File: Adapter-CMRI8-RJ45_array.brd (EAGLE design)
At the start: 100.6 x 107.6 mm, 96 parts

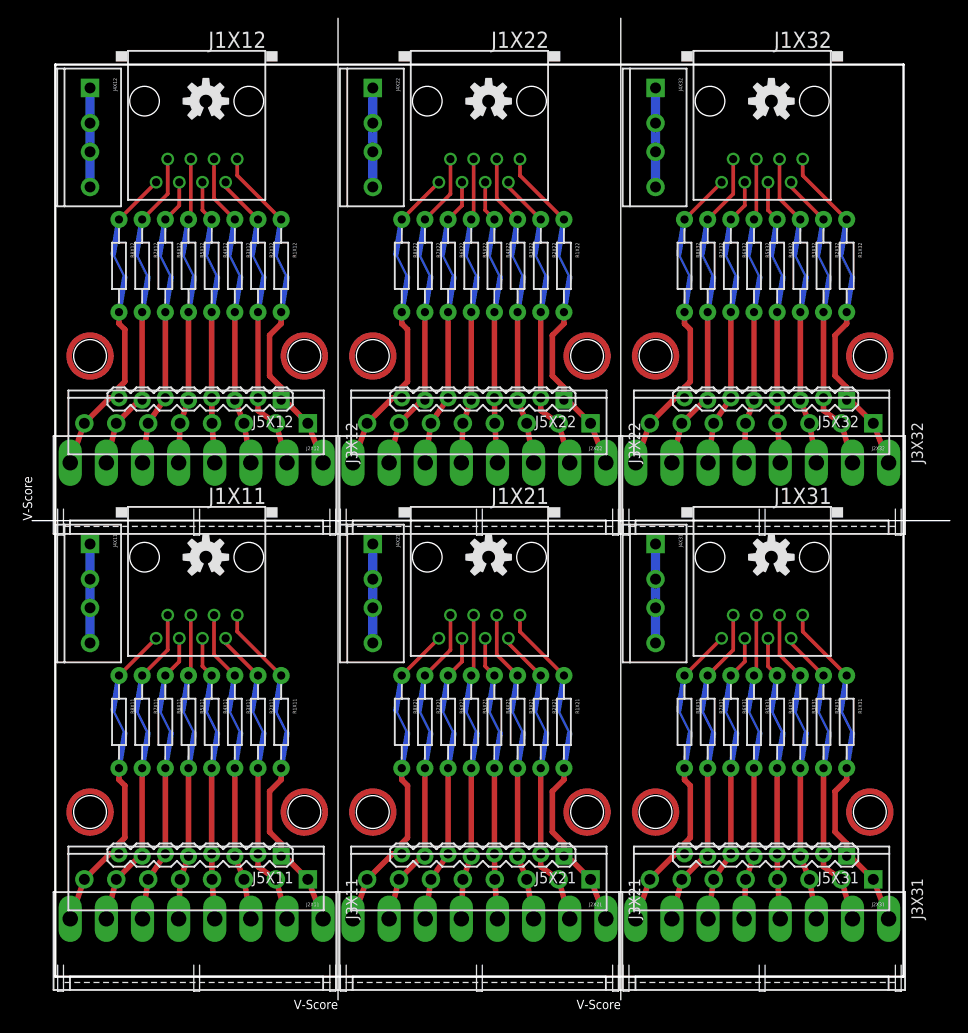
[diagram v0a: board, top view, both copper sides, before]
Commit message: V5.0 added SPDT frog power
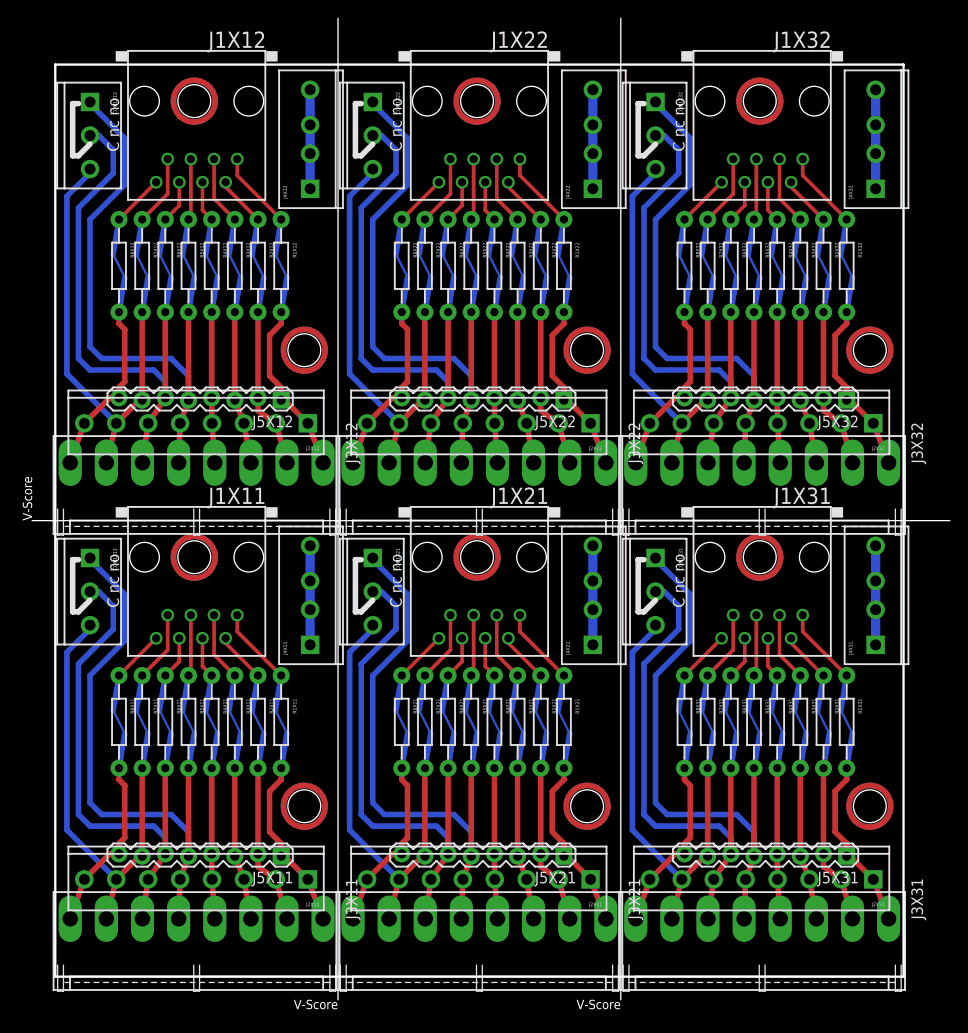
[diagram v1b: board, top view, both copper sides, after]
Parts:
- added CON1X11, CON1X12, CON1X21, CON1X22, CON1X31, CON1X32: CONNECTOR-M033.5MM-LOCK, SPCoast:SCREWTERMINAL-3.5MM-3_LOCK.007S
- J1X11, J1X12, J1X21, J1X22, J1X31, J1X32: value (none) -> RJ45
- M1X11, M1X12, M1X21, M1X22, M1X31, M1X32, M2X11, M2X12, M2X21, M2X22, M2X31, M2X32: value (none) -> MOUNTINGHOLE
- U$1X11, U$1X12, U$1X21, U$1X22, U$1X31, U$1X32: value (none) -> DOC-OSHW-LOGO-L; device SPCoast:OSHW-LOGO-M -> SPCoast:OSHW-LOGO-L
- moved M1X11 30.2 mm to (15.2, 46.0)
- moved M1X21 30.2 mm to (46.2, 46.0)
- moved M1X12 30.2 mm to (15.2, 96.0)
- moved M1X22 30.2 mm to (46.2, 96.0)
- moved M1X31 30.2 mm to (77.2, 46.0)
- moved M1X32 30.2 mm to (77.2, 96.0)
- moved J4X11 26.4 mm to (27.9, 36.6), turned to 90 degrees
- moved J4X12 26.4 mm to (27.9, 86.6), turned to 90 degrees
- moved J4X21 26.4 mm to (58.9, 36.6), turned to 90 degrees
- moved J4X22 26.4 mm to (58.9, 86.6), turned to 90 degrees
- moved J4X31 26.4 mm to (89.9, 36.6), turned to 90 degrees
- moved J4X32 26.4 mm to (89.9, 86.6), turned to 90 degrees
- moved U$1X31 1.27 mm to (77.2, 46.0)
- moved U$1X32 1.27 mm to (77.2, 96.0)
- moved U$1X11 1.27 mm to (15.2, 46.0)
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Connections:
- net L5X11: now also CON1X11.1
- net L5X12: now also CON1X12.1
- net L5X21: now also CON1X21.1
- net L5X22: now also CON1X22.1
- net L5X31: now also CON1X31.1
- net L5X32: now also CON1X32.1
- net L6X11: now also CON1X11.2
- net L6X12: now also CON1X12.2
- net L6X21: now also CON1X21.2
- net L6X22: now also CON1X22.2
- net L6X31: now also CON1X31.2
- net L6X32: now also CON1X32.2
- net L7X11: now also CON1X11.3
- net L7X12: now also CON1X12.3
- net L7X21: now also CON1X21.3
- net L7X22: now also CON1X22.3
- net L7X31: now also CON1X31.3
- net L7X32: now also CON1X32.3
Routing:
- net L5X32: track 34.0 -> 78.7 mm
- net L5X31: track 34.0 -> 78.7 mm
- net L5X22: track 34.0 -> 78.7 mm
- net L5X12: track 34.0 -> 78.7 mm
- net L5X11: track 34.0 -> 78.7 mm
- net L5X21: track 34.0 -> 78.7 mm
- net L6X22: track 32.4 -> 72.4 mm
- net L6X21: track 32.4 -> 72.4 mm
- net L6X12: track 32.4 -> 72.4 mm
- net L6X11: track 32.4 -> 72.4 mm
- net L6X32: track 32.4 -> 72.4 mm
- net L6X31: track 32.4 -> 72.4 mm
- net L7X31: track 36.3 -> 67.1 mm
- net L7X11: track 36.3 -> 67.1 mm
- net L7X21: track 36.3 -> 67.1 mm
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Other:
- board text added: "2020.06"
- board text added: "C nc no"
- board text added: "CON1"
- board text added: "Frog Pwr"
- board text added: "no nc C"
- board text added: "v5.0"
- board text removed: "0.156""
- board text removed: "2018.12"
- board text removed: "Resistor"
- board text removed: "v4.0"

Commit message: added values for connectors
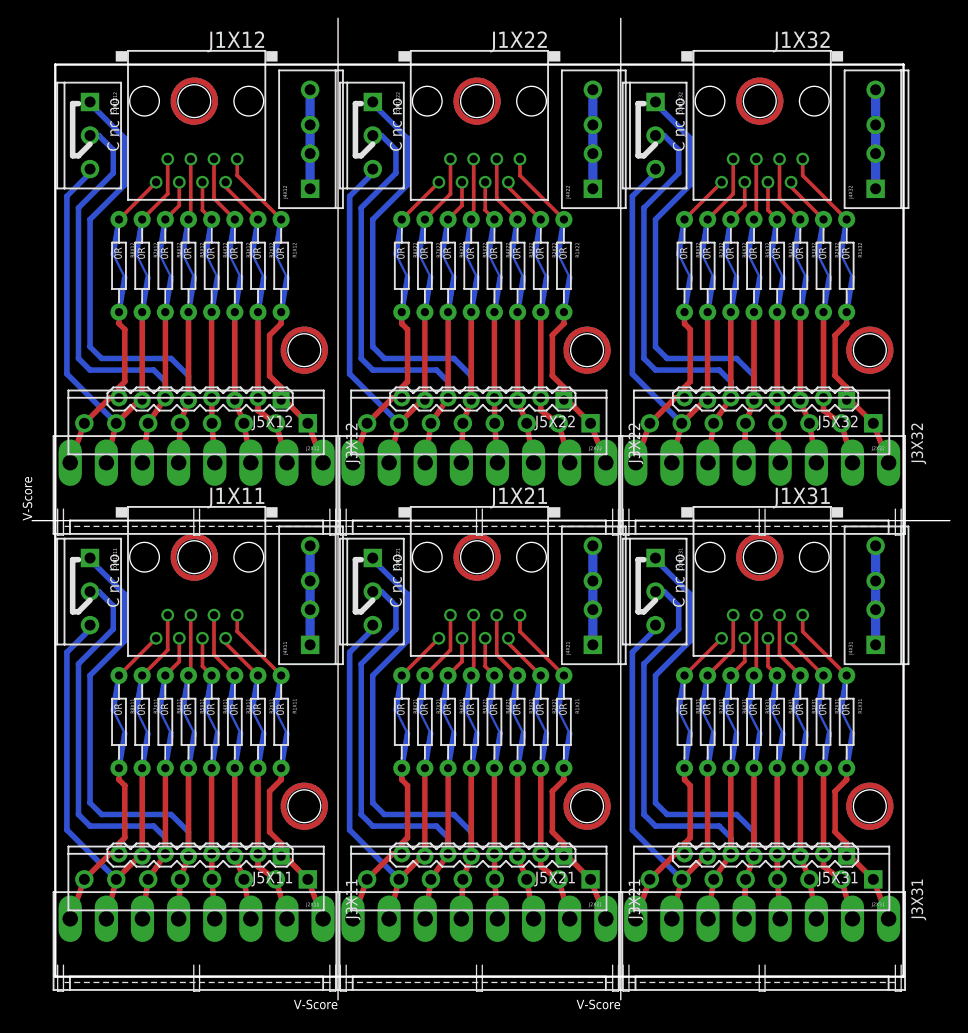
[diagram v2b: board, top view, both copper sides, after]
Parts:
- J2X11, J2X12, J2X21, J2X22, J2X31, J2X32, J4X11, J4X12, J4X21, J4X22, J4X31, J4X32: value (none) -> 3.5mm
- J5X11, J5X12, J5X21, J5X22, J5X31, J5X32: value (none) -> 0.100
- R1X11, R1X12, R1X21, R1X22, R1X31, R1X32, R2X11, R2X12, R2X21, R2X22, R2X31, R2X32, R3X11, R3X12, R3X21, R3X22, R3X31, R3X32, R4X11, R4X12, R4X21, R4X22, R4X31, R4X32, R5X11, R5X12, R5X21, R5X22, R5X31, R5X32, R6X11, R6X12, R6X21, R6X22, R6X31, R6X32, R7X11, R7X12, R7X21, R7X22, R7X31, R7X32, R8X11, R8X12, R8X21, R8X22, R8X31, R8X32: value (none) -> 0R

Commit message: added values for connectors
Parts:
- J3X11, J3X12, J3X21, J3X22, J3X31, J3X32: value (none) -> 0.156
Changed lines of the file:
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@@
 <element name="J1X11" library="SPCoast" package="RJ45-NO-SHIELD" value="RJ45" x="15.5" y="45.99" rot="R180"/>
 <element name="J2X11" library="SPCoast" package="SCREWTERMINAL-3.5MM-8" value="3.5mm" x="27.686" y="10.668" rot="R180"/>
-<element name="J3X11" library="SPCoast" package="KK-156-8-F" value="" x="15.5" y="6.35" rot="R180"/>
+<element name="J3X11" library="SPCoast" package="KK-156-8-F" value="0.156" x="15.5" y="6.35" rot="R180"/>
 <element name="J4X11" library="SPCoast" package="SCREWTERMINAL-3.5MM-4_LOCK" value="3.5mm" x="27.94" y="36.56" rot="R90"/>
 <element name="J5X11" library="SPCoast" package="1X08_LOCK" value="0.100" x="24.765" y="13.335" rot="R180"/>
@@
 <element name="J1X12" library="SPCoast" package="RJ45-NO-SHIELD" value="RJ45" x="15.5" y="95.99" rot="R180"/>
 <element name="J2X12" library="SPCoast" package="SCREWTERMINAL-3.5MM-8" value="3.5mm" x="27.686" y="60.668" rot="R180"/>
-<element name="J3X12" library="SPCoast" package="KK-156-8-F" value="" x="15.5" y="56.35" rot="R180"/>
+<element name="J3X12" library="SPCoast" package="KK-156-8-F" value="0.156" x="15.5" y="56.35" rot="R180"/>
 <element name="J4X12" library="SPCoast" package="SCREWTERMINAL-3.5MM-4_LOCK" value="3.5mm" x="27.94" y="86.56" rot="R90"/>
 <element name="J5X12" library="SPCoast" package="1X08_LOCK" value="0.100" x="24.765" y="63.335" rot="R180"/>
@@
 <element name="J1X21" library="SPCoast" package="RJ45-NO-SHIELD" value="RJ45" x="46.5" y="45.99" rot="R180"/>
 <element name="J2X21" library="SPCoast" package="SCREWTERMINAL-3.5MM-8" value="3.5mm" x="58.686" y="10.668" rot="R180"/>
-<element name="J3X21" library="SPCoast" package="KK-156-8-F" value="" x="46.5" y="6.35" rot="R180"/>
+<element name="J3X21" library="SPCoast" package="KK-156-8-F" value="0.156" x="46.5" y="6.35" rot="R180"/>
 <element name="J4X21" library="SPCoast" package="SCREWTERMINAL-3.5MM-4_LOCK" value="3.5mm" x="58.94" y="36.56" rot="R90"/>
 <element name="J5X21" library="SPCoast" package="1X08_LOCK" value="0.100" x="55.765" y="13.335" rot="R180"/>
@@
 <element name="J1X22" library="SPCoast" package="RJ45-NO-SHIELD" value="RJ45" x="46.5" y="95.99" rot="R180"/>
 <element name="J2X22" library="SPCoast" package="SCREWTERMINAL-3.5MM-8" value="3.5mm" x="58.686" y="60.668" rot="R180"/>
-<element name="J3X22" library="SPCoast" package="KK-156-8-F" value="" x="46.5" y="56.35" rot="R180"/>
+<element name="J3X22" library="SPCoast" package="KK-156-8-F" value="0.156" x="46.5" y="56.35" rot="R180"/>
 <element name="J4X22" library="SPCoast" package="SCREWTERMINAL-3.5MM-4_LOCK" value="3.5mm" x="58.94" y="86.56" rot="R90"/>
 <element name="J5X22" library="SPCoast" package="1X08_LOCK" value="0.100" x="55.765" y="63.335" rot="R180"/>
@@
 <element name="J1X31" library="SPCoast" package="RJ45-NO-SHIELD" value="RJ45" x="77.5" y="45.99" rot="R180"/>
 <element name="J2X31" library="SPCoast" package="SCREWTERMINAL-3.5MM-8" value="3.5mm" x="89.686" y="10.668" rot="R180"/>
-<element name="J3X31" library="SPCoast" package="KK-156-8-F" value="" x="77.5" y="6.35" rot="R180"/>
+<element name="J3X31" library="SPCoast" package="KK-156-8-F" value="0.156" x="77.5" y="6.35" rot="R180"/>
 <element name="J4X31" library="SPCoast" package="SCREWTERMINAL-3.5MM-4_LOCK" value="3.5mm" x="89.94" y="36.56" rot="R90"/>
 <element name="J5X31" library="SPCoast" package="1X08_LOCK" value="0.100" x="86.765" y="13.335" rot="R180"/>
@@
 <element name="J1X32" library="SPCoast" package="RJ45-NO-SHIELD" value="RJ45" x="77.5" y="95.99" rot="R180"/>
 <element name="J2X32" library="SPCoast" package="SCREWTERMINAL-3.5MM-8" value="3.5mm" x="89.686" y="60.668" rot="R180"/>
-<element name="J3X32" library="SPCoast" package="KK-156-8-F" value="" x="77.5" y="56.35" rot="R180"/>
+<element name="J3X32" library="SPCoast" package="KK-156-8-F" value="0.156" x="77.5" y="56.35" rot="R180"/>
 <element name="J4X32" library="SPCoast" package="SCREWTERMINAL-3.5MM-4_LOCK" value="3.5mm" x="89.94" y="86.56" rot="R90"/>
 <element name="J5X32" library="SPCoast" package="1X08_LOCK" value="0.100" x="86.765" y="63.335" rot="R180"/>
